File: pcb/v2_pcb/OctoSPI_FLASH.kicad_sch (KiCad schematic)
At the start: 1 part, among them U4 MX66UW1G45GXDI00

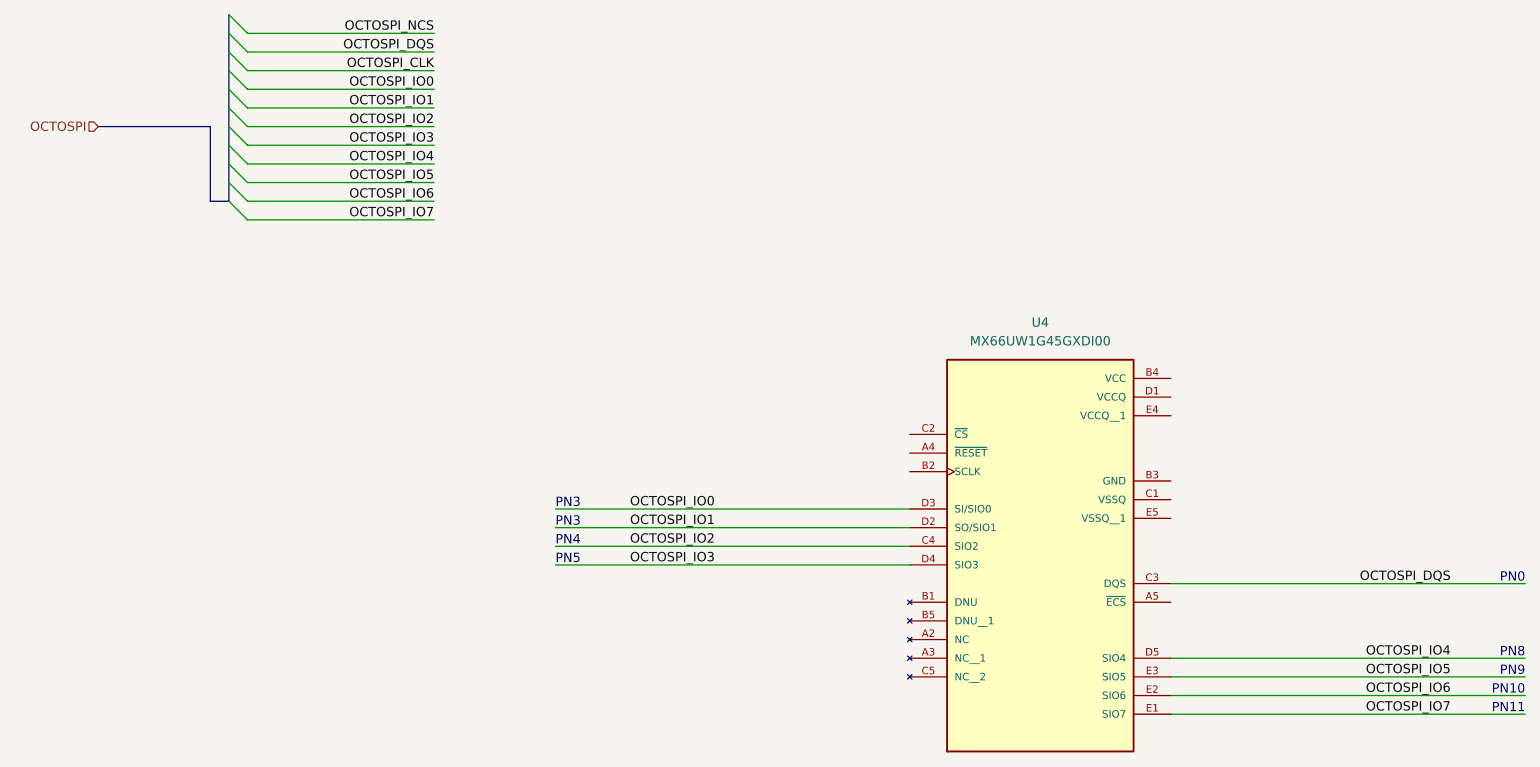
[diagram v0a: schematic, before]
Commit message: add debug to pcb
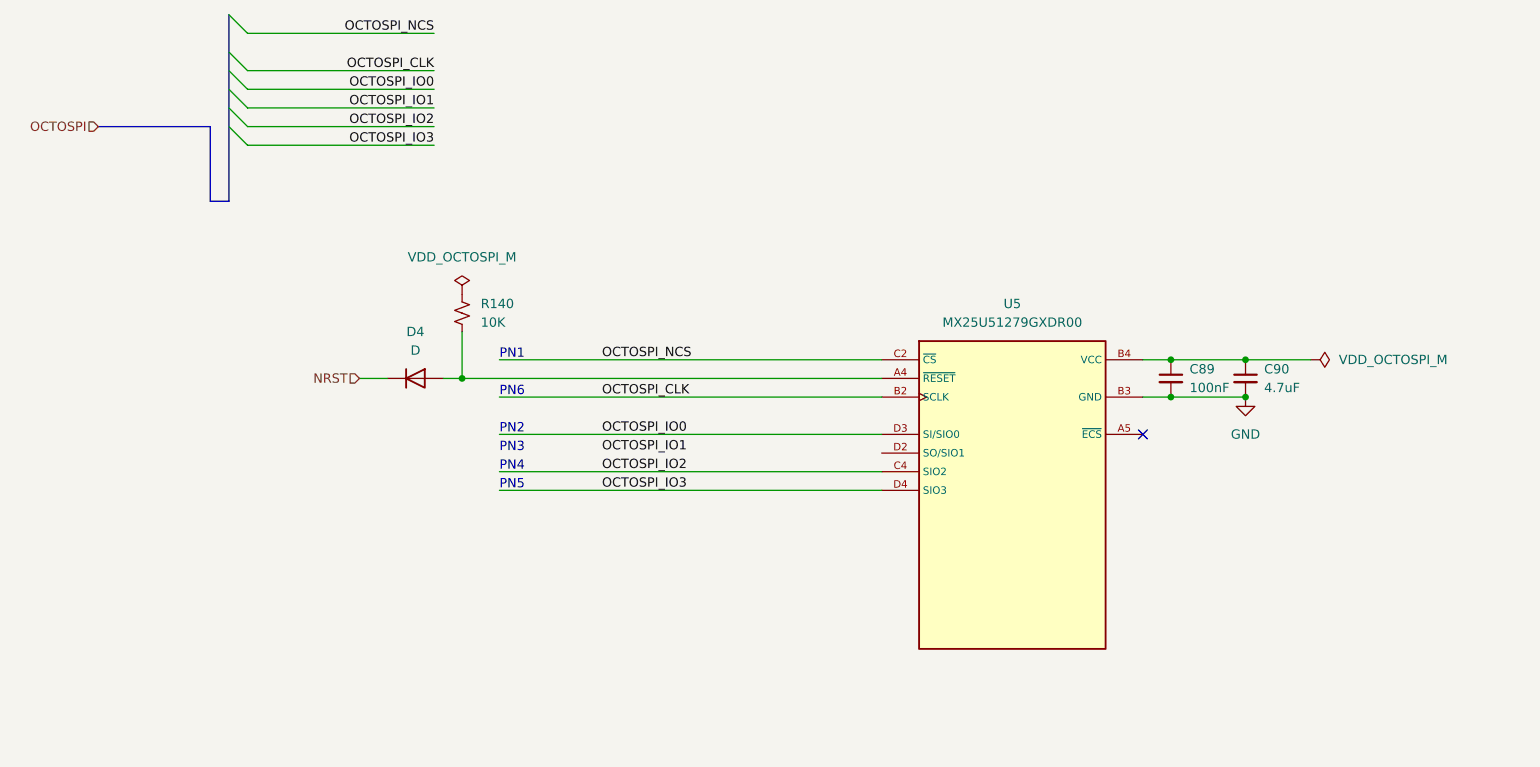
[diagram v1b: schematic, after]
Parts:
- removed U4: MX66UW1G45GXDI00, MX66UW1G45GXDI00:BGA24C100P5X5_800X600X120, symbol noob:MX66UW1G45GXDI00
- added C89: 100nF, symbol Device:C_Small
- added C90: 4.7uF, symbol Device:C_Small
- added D4: D, symbol Device:D
- added R140: 10K, symbol Device:R_Small_US
- added U5: MX25U51279GXDR00, MX66UW1G45GXDI00:BGA24C100P5X5_800X600X120, symbol MX25U51279GXDR00:MX25U51279GXDR00
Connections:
- net OCTOSPI_CLK: now also U5.B2 (SCLK)
- net OCTOSPI_IO0: now also U5.D3 (SI/SIO0)
- net OCTOSPI_IO2: now also U5.C4 (SIO2)
- net OCTOSPI_IO3: now also U5.D4 (SIO3)
- net OCTOSPI_NCS: now also U5.C2 (~{CS})
- new net: D4.2 (A), R140.2, U5.A4 (~{RESET})
- new net: C89.1, C90.1, U5.B4 (VCC)
- new net GND: C89.2, C90.2, U5.B3 (GND)
- new net NRST: D4.1 (K)
- no-connect marks 0 -> 1
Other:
- note added: "PN1"
- note added: "PN2"
- note added: "PN6"
- note removed: "PN0"
- note removed: "PN10"
- note removed: "PN11"
- note removed: "PN8"
- note removed: "PN9"
